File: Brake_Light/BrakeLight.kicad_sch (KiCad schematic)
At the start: 37 parts, among them J2 Conn_01x01_Socket, J3 Conn_01x01_Socket, U1 LM317MABDTG

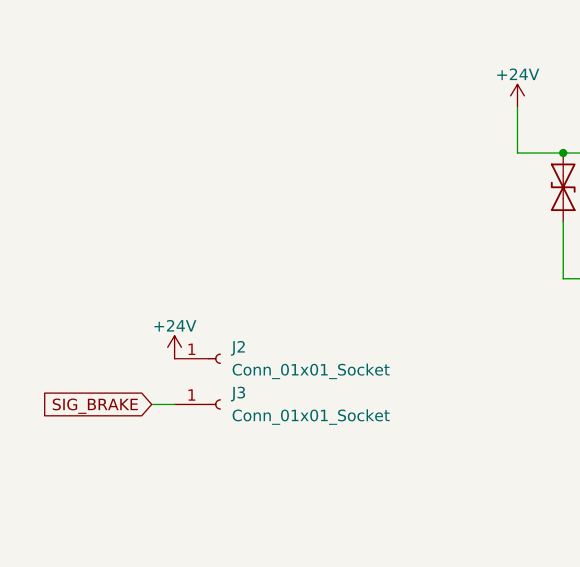
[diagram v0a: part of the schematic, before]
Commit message: Upgrade zones and via
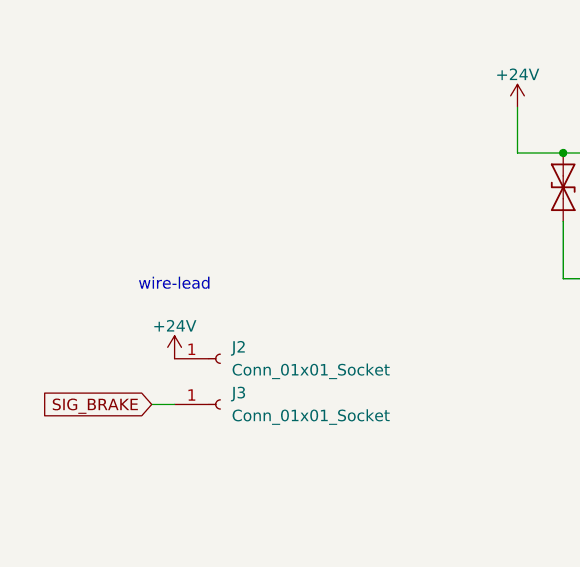
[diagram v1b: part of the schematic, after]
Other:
- note added: "wire-lead"
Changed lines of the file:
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@@
+		)
+	)
+	(text "wire-lead"
+		(exclude_from_sim no)
+		(at 52.07 65.532 0)
+		(effects
+			(font
+				(size 1.27 1.27)
+			)
 		)
 	)
@@
 	(label "ADJ"
 		(at 127 60.96 0)
-		(fields_autoplaced yes)
 		(effects
 			(font
